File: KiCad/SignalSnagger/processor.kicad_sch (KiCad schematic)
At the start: 83 parts, among them J201 Conn_01x01_Female, J202 Conn_01x01_Female, J203 Conn_01x02, J204 Conn_01x02, J205 Conn_01x01_Female, J206 Conn_01x01_Female, J207 Conn_01x01_Female, J210 Conn_01x01_Female, J211 Conn_01x01_Female, J212 Conn_01x01_Female, J213 Conn_01x01_Female, J214 Conn_01x01_Female, J215 Conn_01x01_Female, J216 Conn_01x01_Female, J217 Conn_01x01_Female, J218 Conn_01x02, J219 Conn_01x02, J220 Conn_01x02, J221 Conn_01x02, P201 ISP/PDI, Q201 BSS84W-7-F, Q202 BSS138W-7-F, SW201 SW_SPST, SW202 SW_SPST, SW203 PEC12R-4225F-S0024, SW204 SW_SPST, SW205 SW_SPST, U201 AVR128DA48, U202 SI5351, U203 LP2985-5.0, U204 LP2985-3.3, U205 EA_DOGS104W-A, U206 LP2985-5.0, U207 MAX1683EUK, X202 25 MHz, X901 ECS-327TXO-30-TR

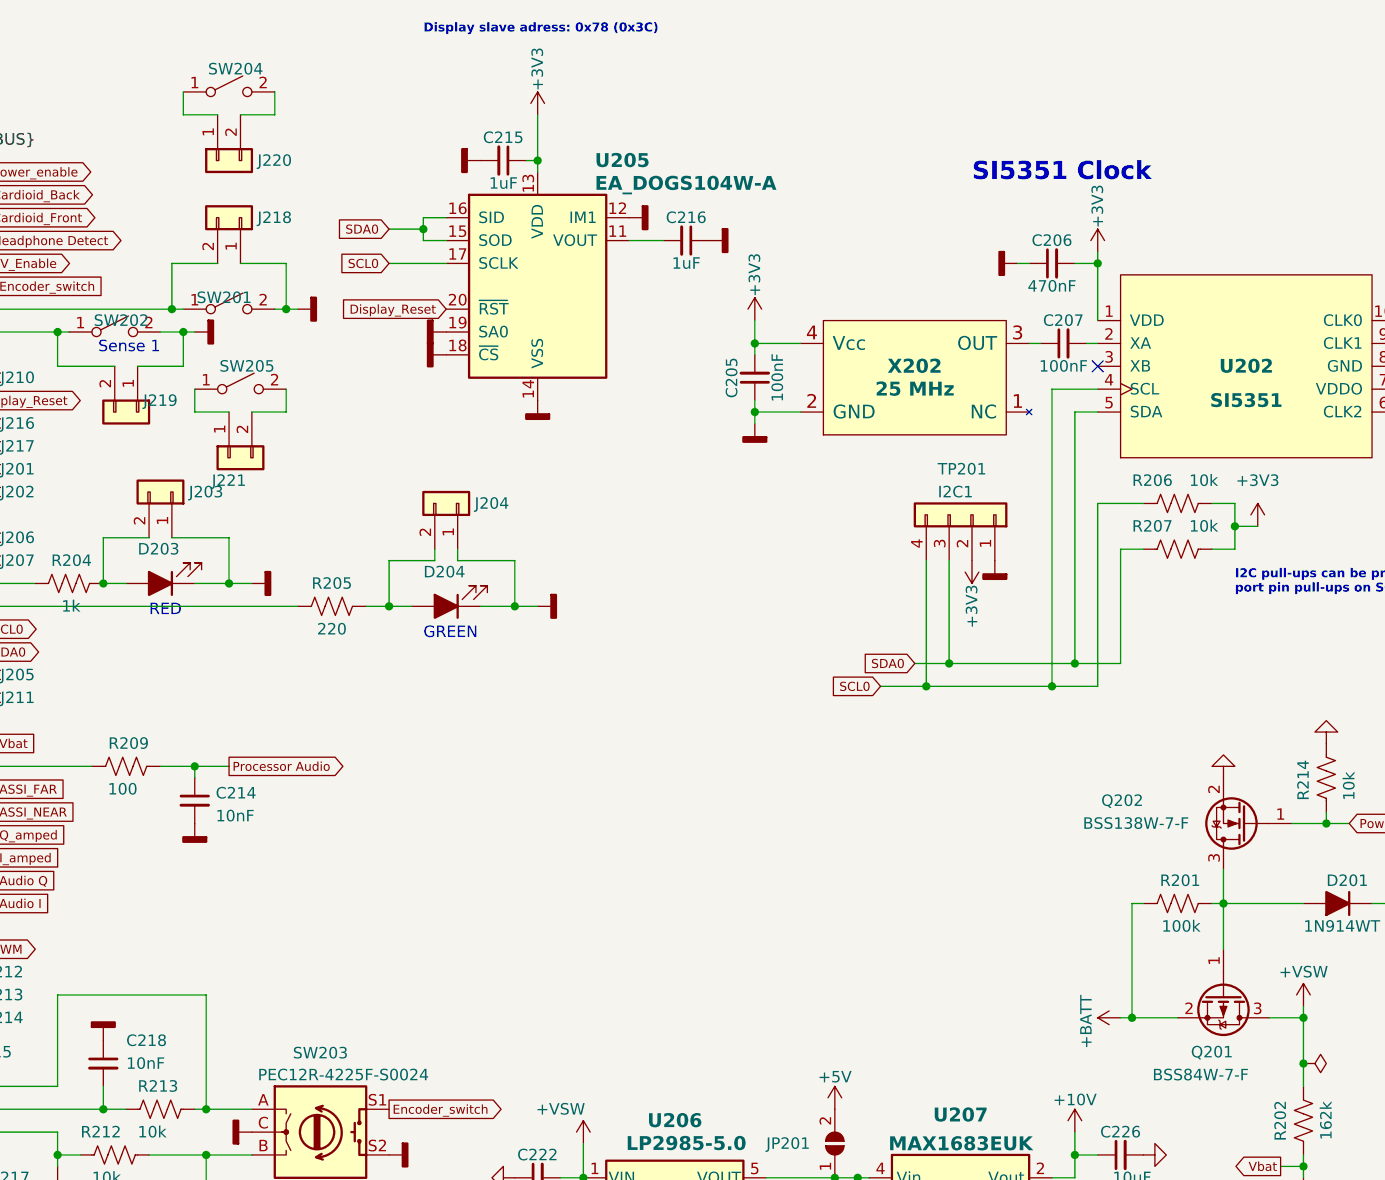
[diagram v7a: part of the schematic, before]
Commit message: Rev 0.313
Schematic, BOM, and PCB updates to add sense switch power-on feature.
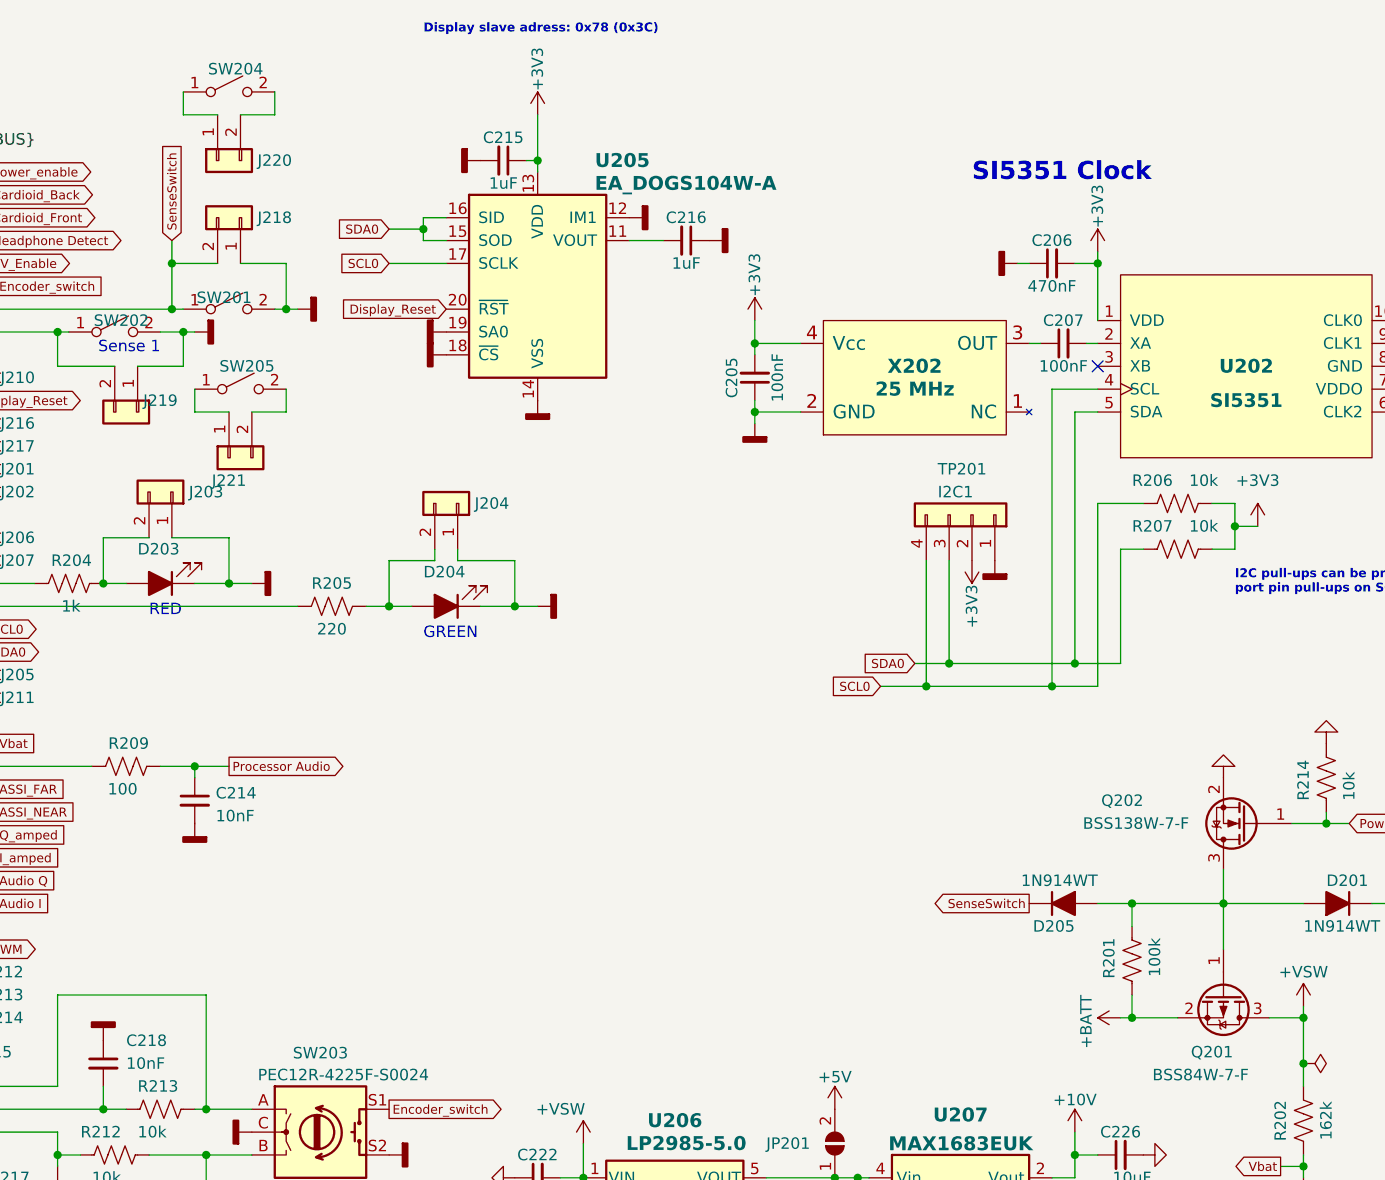
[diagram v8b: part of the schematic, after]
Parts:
- added D205: 1N914WT, Diode_SMD:D_SOD-523, symbol Diode:1N914WT
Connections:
- net at D201.2 (A), Q201.1 (G), Q202.3 (D)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: now also D205.2 (A)
- net PA1 renamed SenseSwitch
- net SenseSwitch: now also D205.1 (K)
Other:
- moved on the sheet: R201
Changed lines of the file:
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@@
     (title "SignalSnagger")
     (date "2024-03-29")
-    (rev "0.312")
+    (rev "0.313")
   )
   (bus_alias "PROC_BUS" (members "PA7" "PA6" "PA5" "PA4" "PA3" "PA2" "PA1" "PA0" "PB5" "PB4" "SCL1" "SDA1" "PB1" "PB0" "PC7" "PC6" "PC5" "PC4" "SCL0" "SDA0" "RXD1" "TXD1" "ADC7" "DAC0" "ADC5" "ADC4" "ADC3" "ADC2" "ADC1" "ADC0" "PE3" "PE2" "RXD4" "TXD4" "PF6" "PF5" "PF4" "PF3" "PF2"))
@@
   (junction (at 31.75 76.2) (diameter 0) (color 0 0 0 0)
   )
+  (junction (at 229.87 121.92) (diameter 0) (color 0 0 0 0)
+  )
+  (junction (at 229.87 134.62) (diameter 0) (color 0 0 0 0)
+  )
   (junction (at 77.47 179.07) (diameter 0) (color 0 0 0 0)
   )
@@
   (junction (at 207.01 97.79) (diameter 0) (color 0 0 0 0)
   )
+  (junction (at 123.19 50.8) (diameter 0) (color 0 0 0 0)
+  )
   (junction (at 123.19 55.88) (diameter 0) (color 0 0 0 0)
   )
@@
   (junction (at 168.91 152.4) (diameter 0) (color 0 0 0 0)
   )
-  (junction (at 229.87 134.62) (diameter 0) (color 0 0 0 0)
-  )
   (junction (at 125.73 106.68) (diameter 0) (color 0 0 0 0)
   )
@@
     (stroke (width 0) (type default) (color 0 0 0 0))
   )
-  (wire (pts (xy 238.76 121.92) (xy 240.03 121.92))
+  (wire (pts (xy 229.87 121.92) (xy 240.03 121.92))
     (stroke (width 0) (type default) (color 0 0 0 0))
   )
@@
     (stroke (width 0) (type default) (color 0 0 0 0))
   )
-  (wire (pts (xy 229.87 134.62) (xy 234.95 134.62))
+  (wire (pts (xy 228.6 134.62) (xy 229.87 134.62))
     (stroke (width 0) (type default) (color 0 0 0 0))
   )
@@
     (stroke (width 0) (type default) (color 0 0 0 0))
   )
-  (bus (pts (xy 96.52 134.62) (xy 96.52 137.16))
+  (wire (pts (xy 229.87 132.08) (xy 229.87 134.62))
     (stroke (width 0) (type default) (color 0 0 0 0))
   )
-  (bus (pts (xy 96.52 147.32) (xy 96.52 149.86))
+  (bus (pts (xy 96.52 134.62) (xy 96.52 137.16))
     (stroke (width 0) (type default) (color 0 0 0 0))
   )
-  (wire (pts (xy 228.6 134.62) (xy 229.87 134.62))
+  (bus (pts (xy 96.52 147.32) (xy 96.52 149.86))
     (stroke (width 0) (type default) (color 0 0 0 0))
   )
@@
     (stroke (width 0) (type default) (color 0 0 0 0))
   )
+  (wire (pts (xy 226.06 121.92) (xy 229.87 121.92))
+    (stroke (width 0) (type default) (color 0 0 0 0))
+  )
   (wire (pts (xy 99.06 104.14) (xy 102.87 104.14))
     (stroke (width 0) (type default) (color 0 0 0 0))
@@
     (stroke (width 0) (type default) (color 0 0 0 0))
   )
+  (wire (pts (xy 123.19 48.26) (xy 123.19 50.8))
+    (stroke (width 0) (type default) (color 0 0 0 0))
+  )
   (wire (pts (xy 110.49 149.86) (xy 110.49 151.13))
     (stroke (width 0) (type default) (color 0 0 0 0))
@@
     (stroke (width 0) (type default) (color 0 0 0 0))
   )
-  (wire (pts (xy 229.87 121.92) (xy 229.87 134.62))
-    (stroke (width 0) (type default) (color 0 0 0 0))
-  )
   (wire (pts (xy 231.14 77.47) (xy 226.06 77.47))
     (stroke (width 0) (type default) (color 0 0 0 0))
@@
     (stroke (width 0) (type default) (color 0 0 0 0))
   )
-  (wire (pts (xy 231.14 121.92) (xy 229.87 121.92))
+  (wire (pts (xy 229.87 124.46) (xy 229.87 121.92))
     (stroke (width 0) (type default) (color 0 0 0 0))
   )
@@
     (stroke (width 0) (type default) (color 0 0 0 0))
   )
+  (wire (pts (xy 229.87 134.62) (xy 234.95 134.62))
+    (stroke (width 0) (type default) (color 0 0 0 0))
+  )
   (wire (pts (xy 130.81 185.42) (xy 130.81 182.88))
     (stroke (width 0) (type default) (color 0 0 0 0))
@@
     )
   )
+  (global_label "SenseSwitch" (shape input) (at 123.19 48.26 90) (fields_autoplaced)
+    (effects (font (size 1 1)) (justify left))
+    (property "Intersheet References" "${INTERSHEET_REFS}" (id 0) (at 123.1275 37.1695 90)
+      (effects (font (size 1 1)) (justify left) hide)
+    )
+  )
+  (global_label "SenseSwitch" (shape output) (at 218.44 121.92 180) (fields_autoplaced)
+    (effects (font (size 1 1)) (justify right))
+    (property "Intersheet References" "${INTERSHEET_REFS}" (id 0) (at 207.3495 121.8575 0)
+      (effects (font (size 1 1)) (justify right) hide)
+    )
+  )
   (global_label "Display_Reset" (shape output) (at 101.6 66.04 0) (fields_autoplaced)
     (effects (font (size 1 1)) (justify left))
@@
     (pin "2")
   )
+  (symbol (lib_id "Diode:1N914WT") (at 222.25 121.92 0) (unit 1)
+    (in_bom yes) (on_board yes)
+    (property "Reference" "D205" (id 0) (at 223.52 124.46 0)
+      (effects (font (size 1.27 1.27)) (justify right))
+    )
+    (property "Value" "1N914WT" (id 1) (at 226.06 119.38 0)
+      (effects (font (size 1.27 1.27)) (justify right))
+    )
+    (property "Footprint" "Diode_SMD:D_SOD-523" (id 2) (at 222.25 126.365 0)
+      (effects (font (size 1.27 1.27)) hide)
+    )
+    (property "Datasheet" "" (id 3) (at 222.25 121.92 0)
+      (effects (font (size 1.27 1.27)) hide)
+    )
+    (property "Digi-Key Part No." "1N4148WTDICT-ND" (id 4) (at 222.25 121.92 0)
+      (effects (font (size 1.27 1.27)) hide)
+    )
+    (property "Link" "https://www.digikey.com/en/products/detail/diodes-incorporated/1N4148WT-7/583731" (id 5) (at 222.25 121.92 0)
+      (effects (font (size 1.27 1.27)) hide)
+    )
+    (property "Manufacturer" "Diodes Incorporated" (id 6) (at 222.25 121.92 0)
+      (effects (font (size 1.27 1.27)) hide)
+    )
+    (property "Manufacturer PN" "1N4148WT-7" (id 7) (at 222.25 121.92 0)
+      (effects (font (size 1.27 1.27)) hide)
+    )
+    (property "Description" "DIODE GEN PURP 80V 125MA SOD523" (id 8) (at 222.25 121.92 0)
+      (effects (font (size 1.27 1.27)) hide)
+    )
+    (property "LCSC Part Number" "C83482" (id 9) (at 222.25 121.92 0)
+      (effects (font (size 1.27 1.27)) hide)
+    )
+    (pin "1")
+    (pin "2")
+  )
   (symbol (lib_id "Connector:Conn_01x01_Generic") (at 104.14 81.28 0) (unit 1)
     (in_bom yes) (on_board yes)
@@
     (pin "3")
   )
-  (symbol (lib_id "Device:R_US") (at 234.95 121.92 90) (unit 1)
+  (symbol (lib_id "Device:R_US") (at 229.87 128.27 180) (unit 1)
     (in_bom yes) (on_board yes)
-    (property "Reference" "R201" (id 0) (at 237.49 119.38 90)
+    (property "Reference" "R201" (id 0) (at 227.33 125.73 90)
       (effects (font (size 1.27 1.27)) (justify left))
     )
-    (property "Value" "100k" (id 1) (at 237.49 124.46 90)
+    (property "Value" "100k" (id 1) (at 232.41 125.73 90)
       (effects (font (size 1.27 1.27)) (justify left))
     )
-    (property "Footprint" "Resistor_SMD:R_0603_1608Metric" (id 2) (at 235.204 120.904 90)
+    (property "Footprint" "Resistor_SMD:R_0603_1608Metric" (id 2) (at 228.854 128.016 90)
       (effects (font (size 1.27 1.27)) hide)
     )
-    (property "Datasheet" "~" (id 3) (at 234.95 121.92 0)
+    (property "Datasheet" "~" (id 3) (at 229.87 128.27 0)
       (effects (font (size 1.27 1.27)) hide)
     )
-    (property "Digi-Key Part No." "311-100KHRCT-ND" (id 4) (at 234.95 121.92 0)
+    (property "Digi-Key Part No." "311-100KHRCT-ND" (id 4) (at 229.87 128.27 0)
       (effects (font (size 1.27 1.27)) hide)
     )
-    (property "Link" "https://www.digikey.com/en/products/detail/yageo/RC0603FR-07100KL/726889" (id 5) (at 234.95 121.92 0)
+    (property "Link" "https://www.digikey.com/en/products/detail/yageo/RC0603FR-07100KL/726889" (id 5) (at 229.87 128.27 0)
       (effects (font (size 1.27 1.27)) hide)
     )
-    (property "Manufacturer" "YAGEO" (id 6) (at 234.95 121.92 0)
+    (property "Manufacturer" "YAGEO" (id 6) (at 229.87 128.27 0)
       (effects (font (size 1.27 1.27)) hide)
     )
-    (property "Manufacturer PN" "RC0603FR-07100KL" (id 7) (at 234.95 121.92 0)
+    (property "Manufacturer PN" "RC0603FR-07100KL" (id 7) (at 229.87 128.27 0)
       (effects (font (size 1.27 1.27)) hide)
     )
-    (property "Description" "RES 100K OHM 1% 1/10W 0603" (id 8) (at 234.95 121.92 0)
+    (property "Description" "RES 100K OHM 1% 1/10W 0603" (id 8) (at 229.87 128.27 0)
       (effects (font (size 1.27 1.27)) hide)
     )
